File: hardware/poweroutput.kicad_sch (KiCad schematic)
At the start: 3 parts, among them J4 DG142R-5.08-02P-14-00AH, J5 108-0902-001, J6 108-0903-001

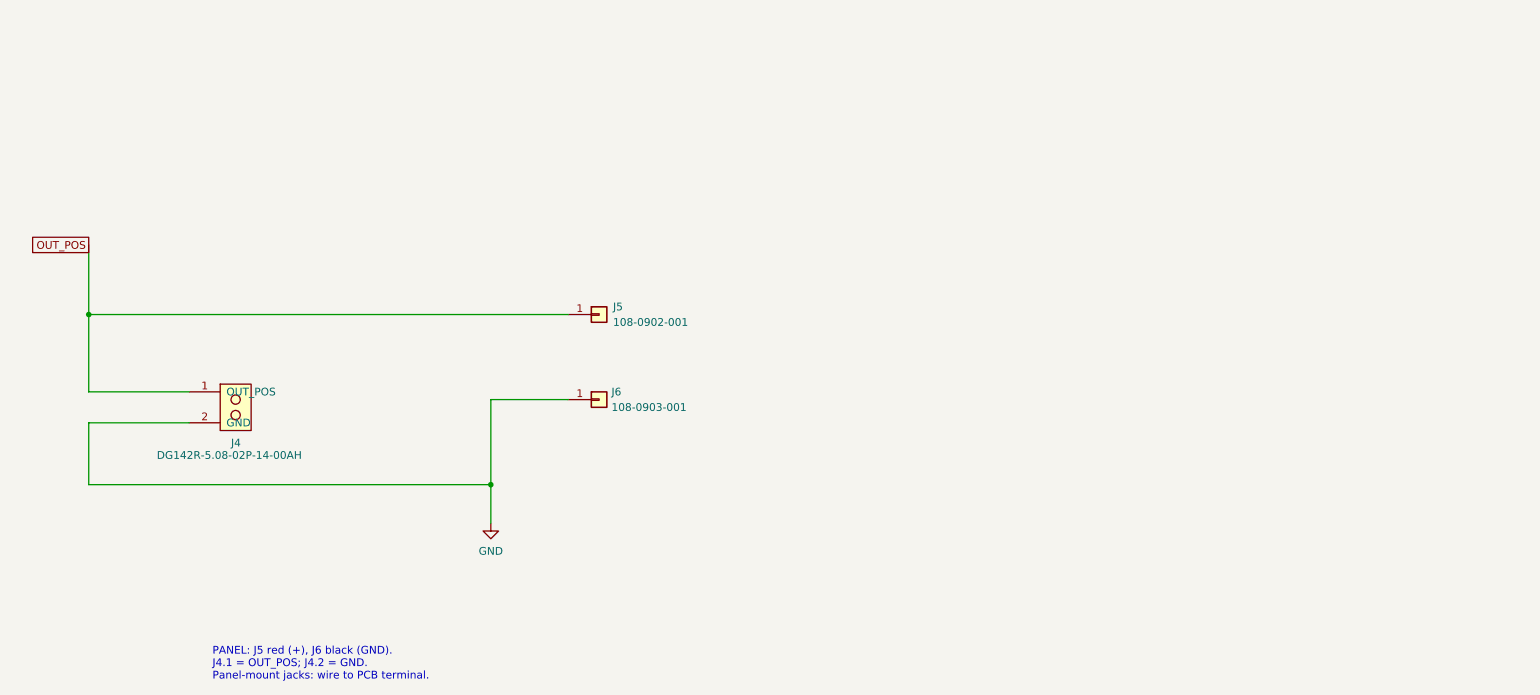
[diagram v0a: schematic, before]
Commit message: poweroutput: AP74502Q kullanıcı çıkış anahtarını ekle (REV_C 3.4, 3.2 #3)
Kullanıcı akımı artık Q3/Q4'ten geçmiyor; şöntün arkasındaki dallanma
noktasından (PD_VBUS_SENSED) M1/M2 back-to-back FET çifti üzerinden akıyor.
Yol kaybı yarıya iniyor.

Bileşenler (14): U12 AP74502Q, Q5/Q6 back-to-back NMOS (60V 4mR TBD),
D6 BZT52C12 GATE-SRC zener, D7 SMBJ30A çıkış TVS, R54 1k + C30 22nF
soft-start, R55/R56 232k/10k OVLO, R57/R58 10k/100k EN ağı, R59 10k bleed,
C31 220nF VCAP, C32 100nF VIN.

OVLO bölücü hesabı: V(OVR) = 1.25 V tip -> 232k/10k = 30.25 V tipik,
tolerans uçlarında 28.2-32.3 V. Bölücü akımı 124 uA, OV kaçağı 110 nA max.

3.2 #3: powersensing'deki PD_VOUT etiketi SW_OUT oldu. INA228 Vin+ ve
RShunt1 artık M2 drain'inden besleniyor, PD_VOUT'tan değil.

Doğrulama (netlist)
- PD_VBUS_SENSED: Q5.3 ve R55.1 eklendi (şönt sonrası dallanma)
- GATE_DRV: U12.6, Q5.1, Q6.1, D6.1, R54.1
- SRC_COMMON: U12.8, Q5.2, Q6.2, D6.2
- SW_OUT: Q6.3, RShunt1.1, U3.10  |  OUT_POS: RShunt1.2, U3.8, U3.9, J4.1, D7.1, R59.1
- INA_ALERT wired-OR: U12.1, U3.3, U2.26, R57.2, R58.1
- PD_VOUT artık RShunt1 ve U3.10 içermiyor

AÇIK: OUT_EN hiçbir yere bağlı değil (ERC isolated_pin_label uyarısı).
ESP32-C6-WROOM-1'in 29 pininin tamamı kullanımda, boş GPIO yok. Doküman
3.5 yeni bir strapping olmayan GPIO istiyor ama pin bütçesi buna uygun
değil. GPIO seçimi firmware ve pin haritasını etkilediği için atanmadı.

Sayfa A4 -> A3.

Co-Authored-By: Claude Opus 5 <noreply@anthropic.com>
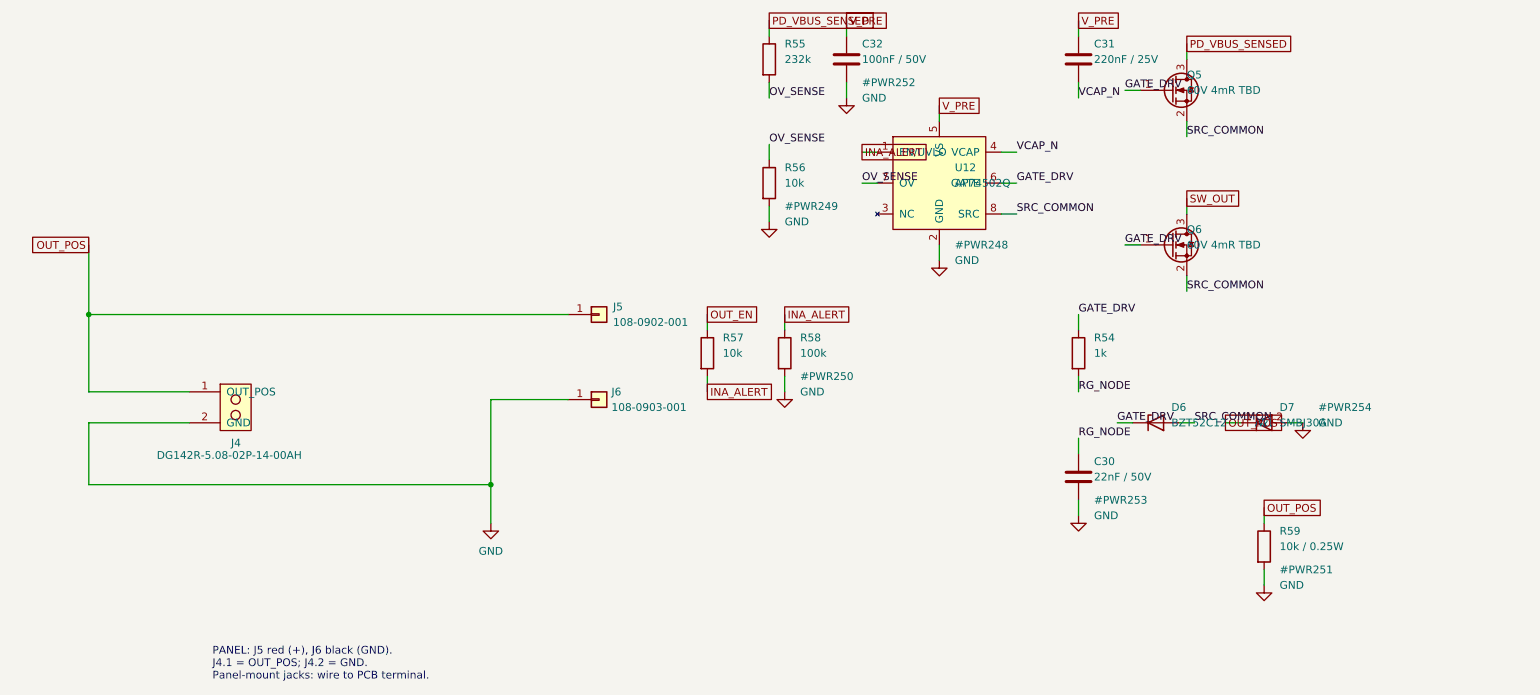
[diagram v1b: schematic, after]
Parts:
- added C30: 22nF / 50V, Capacitor_SMD:C_0402_1005Metric, symbol Device:C
- added C31: 220nF / 25V, Capacitor_SMD:C_0402_1005Metric, symbol Device:C
- added C32: 100nF / 50V, Capacitor_SMD:C_0402_1005Metric, symbol Device:C
- added D6: BZT52C12, Diode_SMD:D_SOD-123, symbol Device:D_Zener
- added D7: SMBJ30A, Diode_SMD:D_SMB, symbol Power_Path_Custom:SMBJ30A
- added Q5, Q6: 60V 4mR TBD, symbol Transistor_FET:Q_NMOS_GSD
- added R54: 1k, Resistor_SMD:R_0402_1005Metric, symbol Device:R
- added R55: 232k, Resistor_SMD:R_0402_1005Metric, symbol Device:R
- added R56, R57: 10k, Resistor_SMD:R_0402_1005Metric, symbol Device:R
- added R58: 100k, Resistor_SMD:R_0402_1005Metric, symbol Device:R
- added R59: 10k / 0.25W, Resistor_SMD:R_0402_1005Metric, symbol Device:R
- added U12: AP74502Q, Package_TO_SOT_SMD:TSOT-23-8_HandSoldering, symbol Power_Path_Custom:AP74502Q
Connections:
- net GND: now also C30.2, C32.2, D7.2 (A2), R56.2, R58.2, R59.2, U12.2 (GND)
- net OUT_POS: now also D7.1 (A1), R59.1
- new net GATE_DRV: D6.1 (K), Q5.1 (G), Q6.1 (G), R54.1, U12.6 (GATE)
- new net INA_ALERT: R57.2, R58.1, U12.1 (EN/UVLO)
- new net OUT_EN: R57.1
- new net OV_SENSE: R55.2, R56.1, U12.7 (OV)
- new net PD_VBUS_SENSED: Q5.3 (D), R55.1
- new net RG_NODE: C30.1, R54.2
- new net SRC_COMMON: D6.2 (A), Q5.2 (S), Q6.2 (S), U12.8 (SRC)
- new net SW_OUT: Q6.3 (D)
- new net VCAP_N: C31.2, U12.4 (VCAP)
- new net V_PRE: C31.1, C32.1, U12.5 (VS)

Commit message: powergeneration: Blok A'yı kistack/schematic skill kurallarına göre yeniden çiz
Izgara + etiket dizilimi yerine gerçek şema yerleşimi. Netlist değişmedi,
ERC 4'te sabit (hepsi REV_C öncesinden).

Yerleşim
- Soldan sağa sinyal akışı: PD_VOUT rayı -> L3 -> BOOST_SW -> D4 -> V_PRE
- Pasifler IC pinlerine gerçek tellerle bağlandı (dekuplaj, SS, FREQ,
  kompanzasyon, EN pull-up). Etiket yalnızca sayfa/blok arası ve okunabilirlik
  düğümlerinde (BOOST_SW, BOOST_FB, V_CL).
- Güç sembolleri: GND aşağı, +3.3V yukarı bakıyor. Referansları (#PWR###)
  gizlendi, değerleri görünür.
- PWR_FLAG kaynağın yanına, D4 çıkışına kondu.
- U11'in AGND/PGND/PowerPAD pinleri tek GND sembolünde köprülendi.
- Renk kodu: PD_VOUT turuncu, BOOST_SW mor, V_PRE kırmızı.
- Blok kesikli dikdörtgen içine alınıp başlıklandırıldı.

Semboller
- Dirençler Device:R_Small_US
- Değerlerde birim: 100kR, 78.7kR, 47nF, 10uF 50V, 6.8uH
- TPS55340PWPR sembolünün kutusu genişletildi (alt pin adları yan pin
  adlarına giriyordu). 15 pinin numara->ad eşlemesi datasheet ile birebir
  doğrulandı, değişmedi.

Yöntem
kicad-cli ile PDF -> pdftoppm ile PNG -> görüntüyü inceleyip düzeltme
döngüsü, 6 tur. Her turda ERC + netlist ile deterministik doğrulama.

Co-Authored-By: Claude Opus 5 <noreply@anthropic.com>
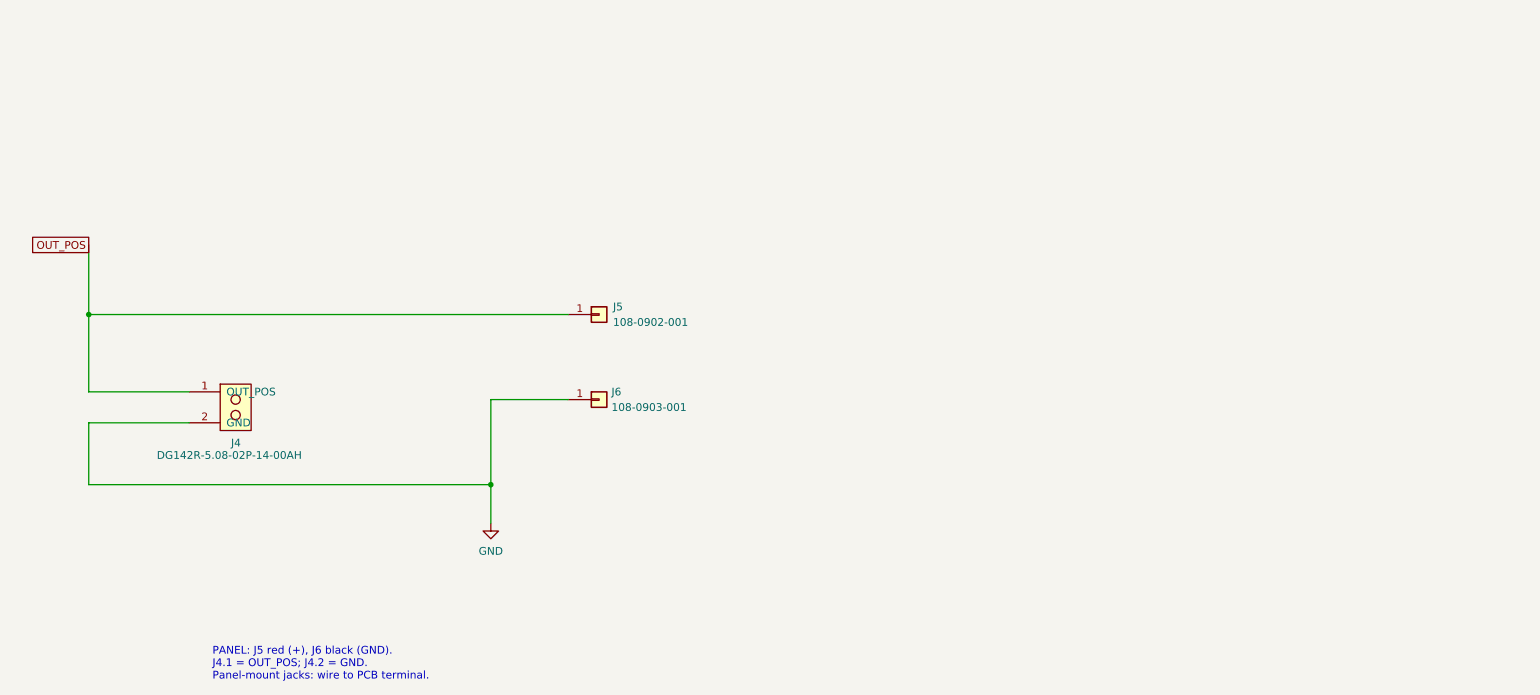
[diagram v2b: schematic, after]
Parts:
- removed C30: 22nF / 50V, Capacitor_SMD:C_0402_1005Metric, symbol Device:C
- removed C31: 220nF / 25V, Capacitor_SMD:C_0402_1005Metric, symbol Device:C
- removed C32: 100nF / 50V, Capacitor_SMD:C_0402_1005Metric, symbol Device:C
- removed D6: BZT52C12, Diode_SMD:D_SOD-123, symbol Device:D_Zener
- removed D7: SMBJ30A, Diode_SMD:D_SMB, symbol Power_Path_Custom:SMBJ30A
- removed Q5, Q6: 60V 4mR TBD, symbol Transistor_FET:Q_NMOS_GSD
- removed R54: 1k, Resistor_SMD:R_0402_1005Metric, symbol Device:R
- removed R55: 232k, Resistor_SMD:R_0402_1005Metric, symbol Device:R
- removed R56, R57: 10k, Resistor_SMD:R_0402_1005Metric, symbol Device:R
- removed R58: 100k, Resistor_SMD:R_0402_1005Metric, symbol Device:R
- removed R59: 10k / 0.25W, Resistor_SMD:R_0402_1005Metric, symbol Device:R
- removed U12: AP74502Q, Package_TO_SOT_SMD:TSOT-23-8_HandSoldering, symbol Power_Path_Custom:AP74502Q

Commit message: poweroutput: Blok B'yi skill kurallarıyla yeniden çiz (REV_C 3.4)
daeca6d commit'i Blok B'yi sessizce geri almıştı: Blok A'nın yerleşimini
yeniden çizerken poweroutput sayfasını da eski haline döndürmüş ve
git add -A onu commit'e dahil etmişti. Bu commit hem o kaybı telafi eder
hem de bloğu profesyonel yerleşimle yeniden kurar.

Yerleşim
- Soldan sağa güç akışı: PD_VBUS_SENSED -> Q5 -> SRC_COMMON -> Q6 -> SW_OUT
- U12 akış hattının altında, gate sürücü ağı sağında
- OVLO bölücü ve EN ağı solda ayrı kolonlarda
- Çıkış koruması (D7 TVS, R59 bleed) sağda
- Renk: PD_VBUS_SENSED turuncu, SW_OUT kırmızı, GATE_DRV mor
- Blok kesikli dikdörtgen içinde, başlıklı

Semboller
- AP74502Q kutusu genişletildi (EN/UVLO ve VCAP pin adları çakışıyordu).
  8 pinin numara->ad eşlemesi datasheet ile birebir, değişmedi.
- Q5 ang 90, Q6 ang 270 (ortak source yatay hatta hizalı)
- Döndürülmüş sembollerde metin prop_rot ile yataya çevrildi

Doğrulama (netlist)
- PD_VBUS_SENSED: Q5.3 ve R55.1 eklendi (şönt sonrası dallanma)
- SRC_COMMON: U12.8, Q5.2, Q6.2, D6.2
- GATE_DRV: U12.6, Q5.1, Q6.1, D6.1, R54.1
- SW_OUT: Q6.3, RShunt1.1, U3.10
- OUT_POS: RShunt1.2, U3.8, U3.9, J4.1, D7.1, R59.1
- INA_ALERT wired-OR: U12.1, U3.3, U2.26, R57.2, R58.1
- V_PRE: U12.5, C31.1, C32.1 eklendi
- ERC 5: dördü REV_C öncesinden, biri OUT_EN'in bağlanmamış olması

Co-Authored-By: Claude Opus 5 <noreply@anthropic.com>
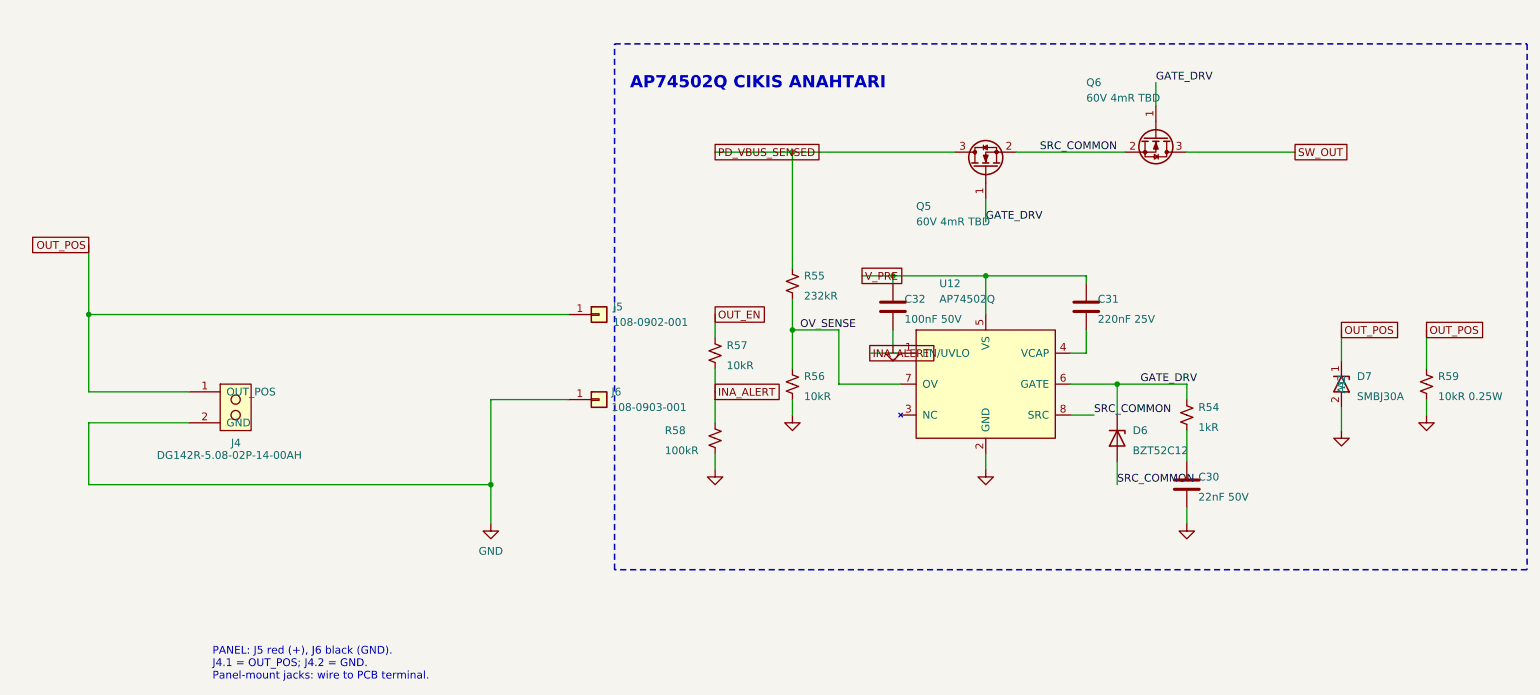
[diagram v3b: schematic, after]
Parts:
- added C30: 22nF 50V, Capacitor_SMD:C_0402_1005Metric, symbol Device:C
- added C31: 220nF 25V, Capacitor_SMD:C_0402_1005Metric, symbol Device:C
- added C32: 100nF 50V, Capacitor_SMD:C_0402_1005Metric, symbol Device:C
- added D6: BZT52C12, Diode_SMD:D_SOD-123, symbol Device:D_Zener
- added D7: SMBJ30A, Diode_SMD:D_SMB, symbol Power_Path_Custom:SMBJ30A
- added Q5, Q6: 60V 4mR TBD, symbol Transistor_FET:Q_NMOS_GSD
- added R54: 1kR, Resistor_SMD:R_0402_1005Metric, symbol Device:R_Small_US
- added R55: 232kR, Resistor_SMD:R_0402_1005Metric, symbol Device:R_Small_US
- added R56, R57: 10kR, Resistor_SMD:R_0402_1005Metric, symbol Device:R_Small_US
- added R58: 100kR, Resistor_SMD:R_0402_1005Metric, symbol Device:R_Small_US
- added R59: 10kR 0.25W, Resistor_SMD:R_0402_1005Metric, symbol Device:R_Small_US
- added U12: AP74502Q, Package_TO_SOT_SMD:TSOT-23-8_HandSoldering, symbol Power_Path_Custom:AP74502Q
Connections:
- net GND: now also C30.2, C32.2, D7.2 (A2), R56.2, R58.2, R59.2, U12.2 (GND)
- net OUT_POS: now also D7.1 (A1), R59.1
- new net: C31.2, U12.4 (VCAP)
- new net: C30.1, R54.2
- new net GATE_DRV: D6.1 (K), Q5.1 (G), Q6.1 (G), R54.1, U12.6 (GATE)
- new net INA_ALERT: R57.2, R58.1, U12.1 (EN/UVLO)
- new net OUT_EN: R57.1
- new net OV_SENSE: R55.2, R56.1, U12.7 (OV)
- new net PD_VBUS_SENSED: Q5.3 (D), R55.1
- new net SRC_COMMON: D6.2 (A), Q5.2 (S), Q6.2 (S), U12.8 (SRC)
- new net SW_OUT: Q6.3 (D)
- new net V_PRE: C31.1, C32.1, U12.5 (VS)
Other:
- note added: "AP74502Q CIKIS ANAHTARI"
